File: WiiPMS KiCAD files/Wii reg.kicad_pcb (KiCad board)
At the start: 4 copper layers, 43.6 x 32.9 mm, 94 parts, among them J11 TEST_1P, J12 TEST_1P, J14 TEST_1P, J16 TEST_1P, J17 TEST_1P, J18 TEST_1P, J24 TEST_1P, J25 Conn_01x05, J26 TEST_1P, J4 TEST_1P, J5 TEST_1P, J8 TEST_1P, Q1 2N3904, Q2 2N3904, Q3 2N3904, U1 tlv62095, U2 tlv62095, U3 TPS61230, U4 tlv62095, U5 tlv62095, U6 PIC16F15324, U7 bq25895m

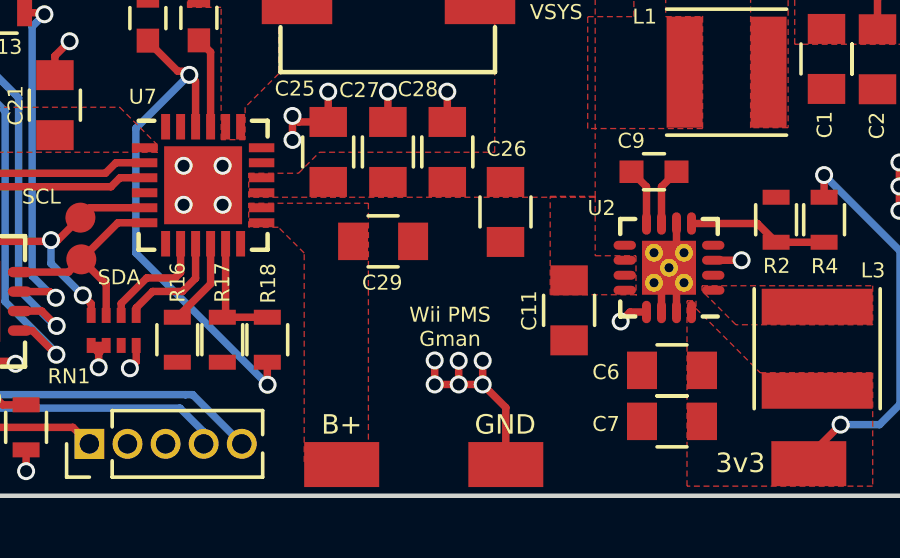
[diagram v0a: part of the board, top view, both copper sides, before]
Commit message: Added STUSB DEVICE_ID_B for compatibility with USBCBoard
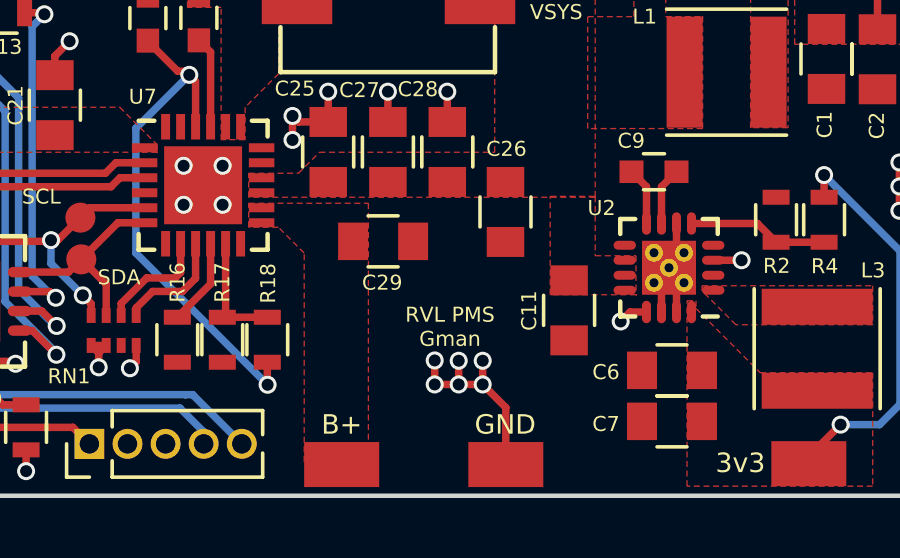
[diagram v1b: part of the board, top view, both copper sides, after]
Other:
- board text added: "RVL PMS Gman"
- board text removed: "Wii PMS Gman"
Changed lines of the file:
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@@
-(kicad_pcb (version 20171130) (host pcbnew "(5.0.1)-4")
+(kicad_pcb (version 20171130) (host pcbnew "(5.1.4)-1")
   (general
     (thickness 1.6)
@@
     (zone_45_only yes)
     (trace_min 0.2)
-    (segment_width 0.2)
-    (edge_width 0.15)
     (via_size 0.6)
     (via_drill 0.4)
@@
     (uvia_min_size 0.2)
     (uvia_min_drill 0.1)
+    (edge_width 0.15)
+    (segment_width 0.2)
     (pcb_text_width 0.3)
     (pcb_text_size 1.5 1.5)
@@
     (effects (font (size 0.5 0.5) (thickness 0.125)))
   )
-  (gr_text "Wii PMS\nGman" (at 212.27 111.76) (layer F.SilkS)
+  (gr_text "RVL PMS\nGman" (at 212.27 111.76) (layer F.SilkS)
     (effects (font (size 0.5 0.5) (thickness 0.125)))
   )
